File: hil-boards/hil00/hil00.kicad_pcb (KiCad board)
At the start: 2 copper layers, 80 x 25 mm, 35 parts, among them J1 USB_C_Receptacle_USB2.0, J2 Conn_01x05_Male, J3 Conn_01x05_Male, Q1 BC847, Q2 BC847, U1 ADUM4160, U2 AMS1117-3.3, U3 CH340G, Y1 Crystal

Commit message: all elements placed
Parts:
- added REF**: MountingHole_3.2mm_M3, MountingHole:MountingHole_3.2mm_M3, F.Cu at (177.0, 128.5)
- added REF**1: MountingHole_3.2mm_M3, MountingHole:MountingHole_3.2mm_M3, F.Cu at (166.8, 128.5)
- added REF**2: MountingHole_3.2mm_M3, MountingHole:MountingHole_3.2mm_M3, F.Cu at (156.7, 128.5)
- added REF**3: MountingHole_3.2mm_M3, MountingHole:MountingHole_3.2mm_M3, F.Cu at (146.5, 128.5)
- added REF**4: MountingHole_3.2mm_M3, MountingHole:MountingHole_3.2mm_M3, F.Cu at (136.4, 128.5)
- added REF**5: MountingHole_3.2mm_M3, MountingHole:MountingHole_3.2mm_M3, F.Cu at (126.2, 128.5)
- added REF**6: MountingHole_3.2mm_M3, MountingHole:MountingHole_3.2mm_M3, F.Cu at (116.0, 128.5)
- added REF**7: MountingHole_3.2mm_M3, MountingHole:MountingHole_3.2mm_M3, F.Cu at (105.9, 128.5)
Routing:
- removed copper zone on B.Cu, net GND1
- removed copper zone on F.Cu, net GND1
- removed copper zone on B.Cu, net GND2
- removed copper zone on F.Cu, net GND2
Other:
- board size 80 x 25 mm -> 82 x 30.5 mm

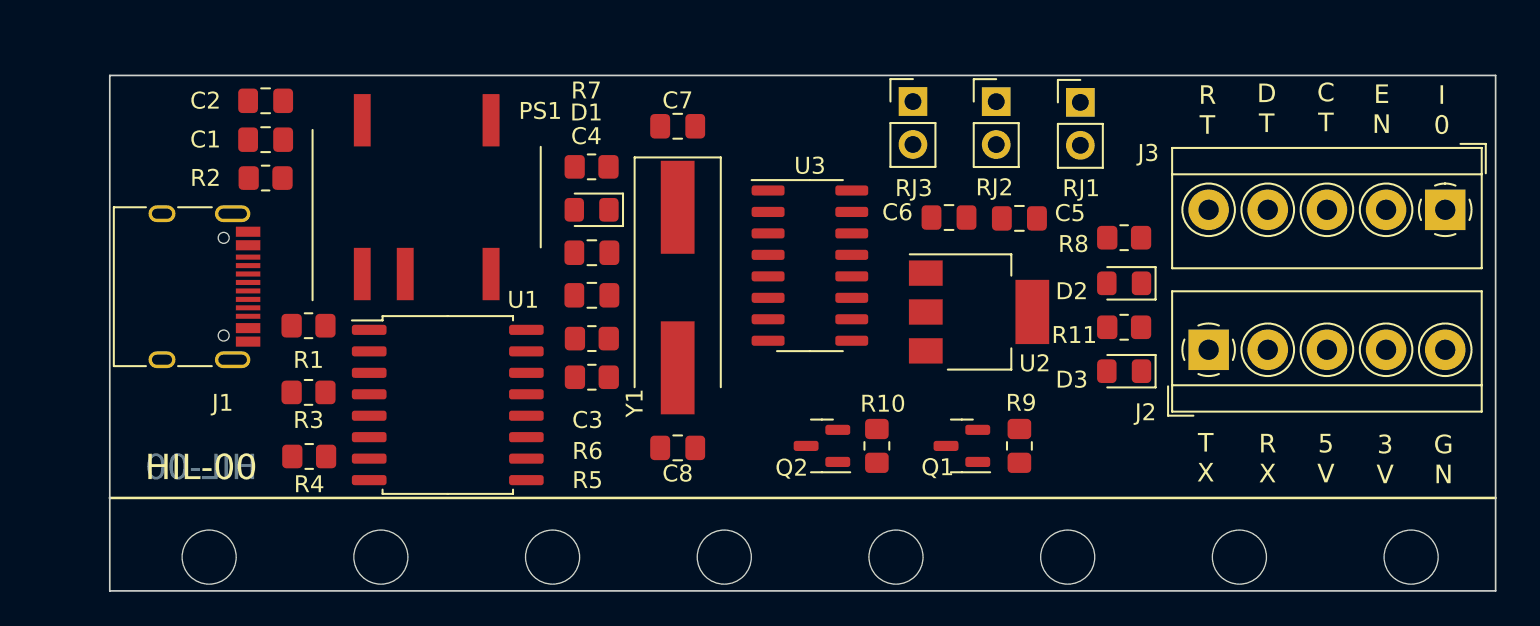
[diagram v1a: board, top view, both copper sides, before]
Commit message: all traces routed
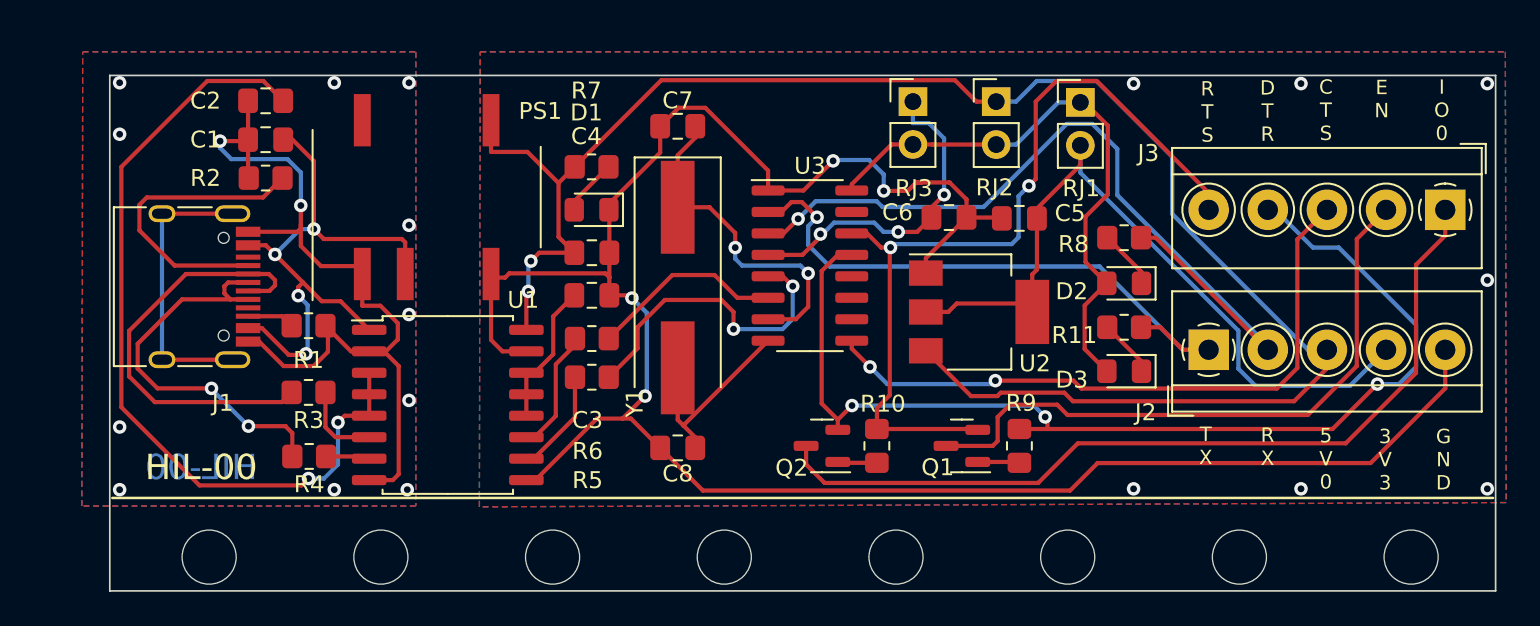
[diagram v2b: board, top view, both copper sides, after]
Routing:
- net GND2: track 0.00 -> 128.5 mm, vias 0 -> 11
- net +5V: track 0.00 -> 102.7 mm, vias 0 -> 2
- net /DTR: track 0.00 -> 64.7 mm, vias 0 -> 3
- net GND1: track 0.00 -> 52.1 mm, vias 0 -> 13
- net /IO0: track 0.00 -> 50.7 mm
- net /RTS: track 0.00 -> 50.5 mm, vias 0 -> 2
- net /RX: track 0.00 -> 50.1 mm, vias 0 -> 1
- net Net-(C2-Pad1): track 0.00 -> 48.7 mm, vias 0 -> 2
- net +3.3V: track 0.00 -> 44.7 mm
- net /CTS: track 0.00 -> 38.6 mm, vias 0 -> 2
- net /EN: track 0.00 -> 37.6 mm
- net /TX: track 0.00 -> 36.2 mm, vias 0 -> 1
- net Net-(C1-Pad1): track 0.00 -> 34.9 mm, vias 0 -> 4
- net VCC: track 0.00 -> 34.8 mm
- net Net-(J1-PadA7): track 0.00 -> 25.4 mm
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- added copper zone on B.Cu, net GND1
- added copper zone on F.Cu, net GND1
- added copper zone on B.Cu, net GND2
- added copper zone on F.Cu, net GND2
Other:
- board text added: "3 V 3"
- board text added: "5 V 0"
- board text added: "C T S"
- board text added: "D T R"
- board text added: "G N D"
- board text added: "I O 0"
- board text added: "R T S"
- board text removed: "3 V"
- board text removed: "5 V"
- board text removed: "C T"
- board text removed: "D T"
- board text removed: "G N"
- board text removed: "I 0"
- board text removed: "R T"

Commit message: improved vias on ground planes
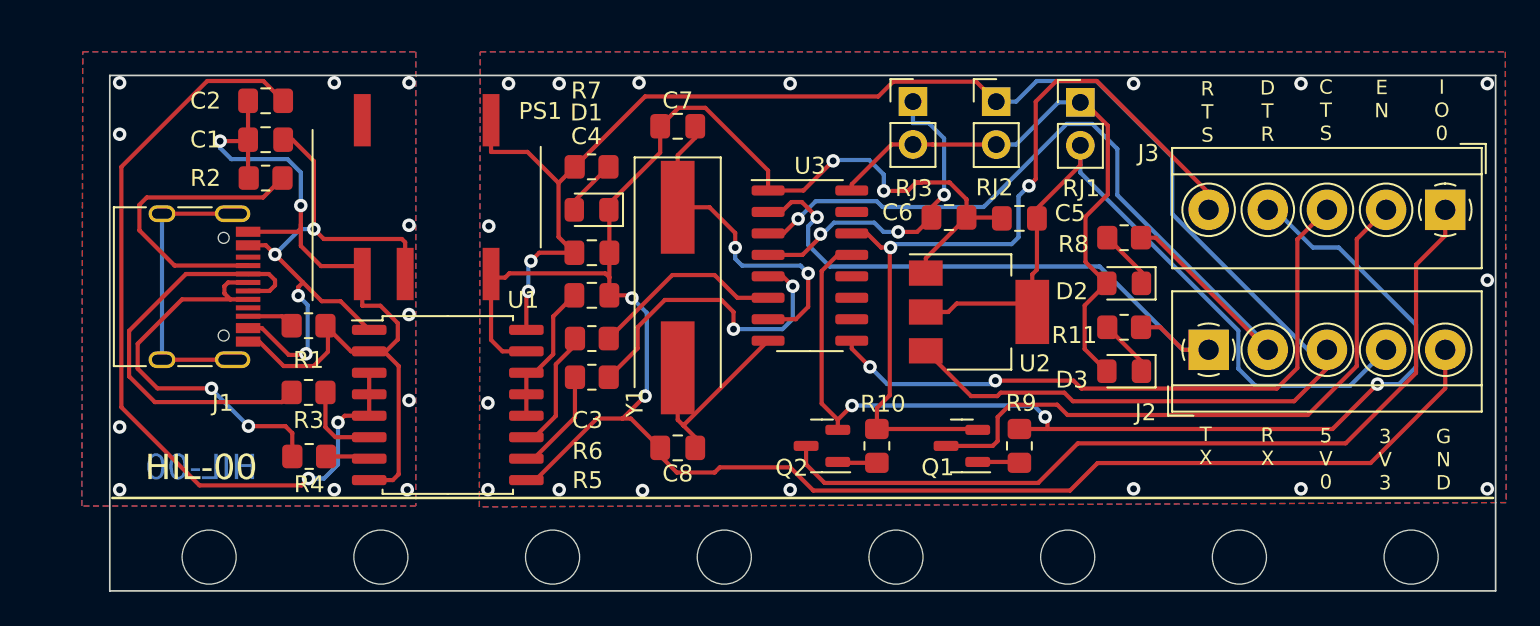
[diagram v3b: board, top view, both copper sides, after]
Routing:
- net GND2: track 128.5 -> 129.0 mm, vias 11 -> 21
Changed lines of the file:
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@@
   (segment (start 124.65 116.325) (end 123.2338 116.325) (width 0.25) (layer "F.Cu") (net 5))
   (segment (start 129.533 107.95) (end 129.533 107.5994) (width 0.25) (layer "F.Cu") (net 5))
-  (segment (start 156.8196 124.5616) (end 158.4452 122.936) (width 0.25) (layer "F.Cu") (net 5))
   (segment (start 123.64391 111.7092) (end 123.391555 111.961555) (width 0.25) (layer "F.Cu") (net 5))
   (segment (start 129.5615 107.9785) (end 129.5615 110.49) (width 0.25) (layer "F.Cu") (net 5))
@@
   (segment (start 123.2338 116.325) (end 122.56 115.6512) (width 0.25) (layer "F.Cu") (net 5))
   (segment (start 145.796 106.8324) (end 147.2184 106.8324) (width 0.25) (layer "F.Cu") (net 5))
+  (segment (start 132.5665 122.5081) (end 133.5532 123.4948) (width 0.25) (layer "F.Cu") (net 5))
+  (segment (start 135.7884 123.4948) (end 136.0932 123.19) (width 0.25) (layer "F.Cu") (net 5))
   (segment (start 130.8329 120.3034) (end 132.5665 122.037) (width 0.25) (layer "F.Cu") (net 5))
   (segment (start 147.7189 106.3319) (end 148.0237 106.3319) (width 0.25) (layer "F.Cu") (net 5))
   (segment (start 131.6736 118.9736) (end 130.3438 120.3034) (width 0.25) (layer "F.Cu") (net 5))
   (segment (start 125.1813 123.945) (end 128.8229 120.3034) (width 0.25) (layer "F.Cu") (net 5))
-  (segment (start 174.5996 122.936) (end 179.0192 118.5164) (width 0.25) (layer "F.Cu") (net 5))
-  (segment (start 179.0192 118.5164) (end 179.0192 116.232) (width 0.25) (layer "F.Cu") (net 5))
+  (segment (start 140.2588 123.19) (end 141.6304 124.5616) (width 0.25) (layer "F.Cu") (net 5))
+  (segment (start 132.5665 122.037) (end 132.5665 122.5081) (width 0.25) (layer "F.Cu") (net 5))
   (segment (start 122.771555 111.961555) (end 122.56 111.75) (width 0.25) (layer "F.Cu") (net 5))
   (segment (start 148.2848 111.6952) (end 148.2848 110.8167) (width 0.25) (layer "F.Cu") (net 5))
   (segment (start 142.7988 105.0544) (end 141.0462 106.807) (width 0.25) (layer "F.Cu") (net 5))
-  (segment (start 132.5665 122.037) (end 135.0911 124.5616) (width 0.25) (layer "F.Cu") (net 5))
   (segment (start 124.65 123.945) (end 125.1813 123.945) (width 0.25) (layer "F.Cu") (net 5))
   (segment (start 148.2848 110.8167) (end 150.6943 108.4072) (width 0.25) (layer "F.Cu") (net 5))
   (segment (start 132.5665 104.5659) (end 132.5665 103.007) (width 0.25) (layer "F.Cu") (net 5))
   (segment (start 129.5615 110.49) (end 129.5615 111.9509) (width 0.25) (layer "F.Cu") (net 5))
+  (segment (start 141.6304 124.5616) (end 156.8196 124.5616) (width 0.25) (layer "F.Cu") (net 5))
+  (segment (start 156.8196 124.5616) (end 158.4452 122.936) (width 0.25) (layer "F.Cu") (net 5))
   (segment (start 129.533 107.5994) (end 132.5665 104.5659) (width 0.25) (layer "F.Cu") (net 5))
   (segment (start 129.5615 111.9509) (end 129.3198 111.7092) (width 0.25) (layer "F.Cu") (net 5))
@@
   (segment (start 130.899301 113.170101) (end 130.7392 113.01) (width 0.25) (layer "F.Cu") (net 5))
   (segment (start 129.533 107.95) (end 129.5615 107.9785) (width 0.25) (layer "F.Cu") (net 5))
+  (segment (start 174.5996 122.936) (end 179.0192 118.5164) (width 0.25) (layer "F.Cu") (net 5))
   (segment (start 138.9522 105.6291) (end 135.2367 101.9136) (width 0.25) (layer "F.Cu") (net 5))
-  (segment (start 135.0911 124.5616) (end 156.8196 124.5616) (width 0.25) (layer "F.Cu") (net 5))
   (segment (start 147.2184 106.8324) (end 147.7189 106.3319) (width 0.25) (layer "F.Cu") (net 5))
   (segment (start 128.8229 120.3034) (end 130.3438 120.3034) (width 0.25) (layer "F.Cu") (net 5))
   (segment (start 141.0462 106.807) (end 138.9522 106.807) (width 0.25) (layer "F.Cu") (net 5))
+  (segment (start 179.0192 118.5164) (end 179.0192 116.232) (width 0.25) (layer "F.Cu") (net 5))
   (segment (start 129.3198 111.7092) (end 123.64391 111.7092) (width 0.25) (layer "F.Cu") (net 5))
   (segment (start 152.7341 108.4072) (end 152.7849 108.458) (width 0.25) (layer "F.Cu") (net 5))
-  (segment (start 158.4452 122.936) (end 174.5996 122.936) (width 0.25) (layer "F.Cu") (net 5))
+  (segment (start 136.0932 123.19) (end 140.2588 123.19) (width 0.25) (layer "F.Cu") (net 5))
+  (segment (start 133.5532 123.4948) (end 135.7884 123.4948) (width 0.25) (layer "F.Cu") (net 5))
   (segment (start 138.9522 106.807) (end 138.9522 105.6291) (width 0.25) (layer "F.Cu") (net 5))
   (segment (start 150.6943 107.334) (end 149.6922 106.3319) (width 0.25) (layer "F.Cu") (net 5))
+  (segment (start 158.4452 122.936) (end 174.5996 122.936) (width 0.25) (layer "F.Cu") (net 5))
   (segment (start 123.391555 111.961555) (end 122.771555 111.961555) (width 0.25) (layer "F.Cu") (net 5))
   (segment (start 130.7392 113.01) (end 129.5615 113.01) (width 0.25) (layer "F.Cu") (net 5))
@@
   (via (at 131.6736 118.9736) (size 0.8) (drill 0.4) (layers "F.Cu" "B.Cu") (net 5))
   (via (at 160.5788 124.46) (size 0.8) (drill 0.4) (layers "F.Cu" "B.Cu") (free) (net 5))
+  (via (at 122.428 108.9152) (size 0.8) (drill 0.4) (layers "F.Cu" "B.Cu") (free) (net 5))
+  (via (at 140.2588 100.4824) (size 0.8) (drill 0.4) (layers "F.Cu" "B.Cu") (free) (net 5))
   (via (at 145.796 106.8324) (size 0.8) (drill 0.4) (layers "F.Cu" "B.Cu") (net 5))
+  (via (at 131.5212 124.5616) (size 0.8) (drill 0.4) (layers "F.Cu" "B.Cu") (free) (net 5))
   (via (at 170.4848 124.46) (size 0.8) (drill 0.4) (layers "F.Cu" "B.Cu") (free) (net 5))
+  (via (at 126.5936 124.5108) (size 0.8) (drill 0.4) (layers "F.Cu" "B.Cu") (free) (net 5))
+  (via (at 131.318 100.4316) (size 0.8) (drill 0.4) (layers "F.Cu" "B.Cu") (free) (net 5))
+  (via (at 123.5964 100.4824) (size 0.8) (drill 0.4) (layers "F.Cu" "B.Cu") (free) (net 5))
+  (via (at 122.3772 124.5108) (size 0.8) (drill 0.4) (layers "F.Cu" "B.Cu") (free) (net 5))
   (via (at 160.5788 100.4824) (size 0.8) (drill 0.4) (layers "F.Cu" "B.Cu") (free) (net 5))
   (via (at 181.5084 100.4824) (size 0.8) (drill 0.4) (layers "F.Cu" "B.Cu") (free) (net 5))
   (via (at 130.899301 113.170101) (size 0.8) (drill 0.4) (layers "F.Cu" "B.Cu") (net 5))
   (via (at 170.4848 100.4824) (size 0.8) (drill 0.4) (layers "F.Cu" "B.Cu") (free) (net 5))
+  (via (at 140.2588 124.5108) (size 0.8) (drill 0.4) (layers "F.Cu" "B.Cu") (free) (net 5))
   (via (at 142.7988 105.0544) (size 0.8) (drill 0.4) (layers "F.Cu" "B.Cu") (net 5))
+  (via (at 122.3772 119.38) (size 0.8) (drill 0.4) (layers "F.Cu" "B.Cu") (free) (net 5))
   (via (at 181.5084 124.46) (size 0.8) (drill 0.4) (layers "F.Cu" "B.Cu") (free) (net 5))
   (via (at 181.5084 112.1156) (size 0.8) (drill 0.4) (layers "F.Cu" "B.Cu") (free) (net 5))
+  (via (at 126.5936 100.4824) (size 0.8) (drill 0.4) (layers "F.Cu" "B.Cu") (free) (net 5))
   (segment (start 142.8496 105.0036) (end 142.7988 105.0544) (width 0.25) (layer "B.Cu") (net 5))
   (segment (start 131.6736 118.9736) (end 131.7752 118.872) (width 0.25) (layer "B.Cu") (net 5))
@@
   (segment (start 124.65 121.405) (end 125.1361 121.405) (width 0.25) (layer "F.Cu") (net 32))
   (segment (start 127.524 115.9604) (end 127.524 115.57) (width 0.25) (layer "F.Cu") (net 32))
+  (segment (start 127.508 105.41) (end 131.6736 101.2444) (width 0.25) (layer "F.Cu") (net 33))
   (segment (start 152.510905 118.9736) (end 150.9632 118.9736) (width 0.25) (layer "F.Cu") (net 33))
   (segment (start 172.0192 116.232) (end 172.0192 117.3376) (width 0.25) (layer "F.Cu") (net 33))
+  (segment (start 151.2708 100.3692) (end 152.4508 101.5492) (width 0.25) (layer "F.Cu") (net 33))
+  (segment (start 131.6736 101.2444) (end 145.473 101.2444) (width 0.25) (layer "F.Cu") (net 33))
   (segment (start 126.5539 106.3641) (end 127.508 105.41) (width 0.25) (layer "F.Cu") (net 33))
   (segment (start 124.65 112.8908) (end 124.7648 112.776) (width 0.25) (layer "F.Cu") (net 33))
-  (segment (start 132.6388 100.2792) (end 150.0055 100.2792) (width 0.25) (layer "F.Cu") (net 33))
-  (segment (start 150.0055 100.2792) (end 151.2755 101.5492) (width 0.25) (layer "F.Cu") (net 33))
   (segment (start 172.0192 117.3376) (end 170.0784 119.2784) (width 0.25) (layer "F.Cu") (net 33))
   (segment (start 122.56 104.5253) (end 124.7151 104.5253) (width 0.25) (layer "F.Cu") (net 33))
   (segment (start 126.5539 109.5574) (end 126.5539 106.3641) (width 0.25) (layer "F.Cu") (net 33))
   (segment (start 150.9632 118.9736) (end 148.2848 116.2952) (width 0.25) (layer "F.Cu") (net 33))
-  (segment (start 151.2755 101.5492) (end 152.4508 101.5492) (width 0.25) (layer "F.Cu") (net 33))
+  (segment (start 146.3482 100.3692) (end 151.2708 100.3692) (width 0.25) (layer "F.Cu") (net 33))
   (segment (start 156.4824 118.7704) (end 152.714105 118.7704) (width 0.25) (layer "F.Cu") (net 33))
+  (segment (start 145.473 101.2444) (end 146.3482 100.3692) (width 0.25) (layer "F.Cu") (net 33))
   (segment (start 124.9172 110.9847) (end 125.4119 110.49) (width 0.25) (layer "F.Cu") (net 33))
   (segment (start 124.7151 104.5253) (end 126.5539 106.3641) (width 0.25) (layer "F.Cu") (net 33))
   (segment (start 170.0784 119.2784) (end 156.9904 119.2784) (width 0.25) (layer "F.Cu") (net 33))
-  (segment (start 127.508 105.41) (end 132.6388 100.2792) (width 0.25) (layer "F.Cu") (net 33))
   (segment (start 122.56 102.65) (end 122.56 104.5253) (width 0.25) (layer "F.Cu") (net 33))
   (segment (start 125.4119 110.49) (end 127.4865 110.49) (width 0.25) (layer "F.Cu") (net 33))

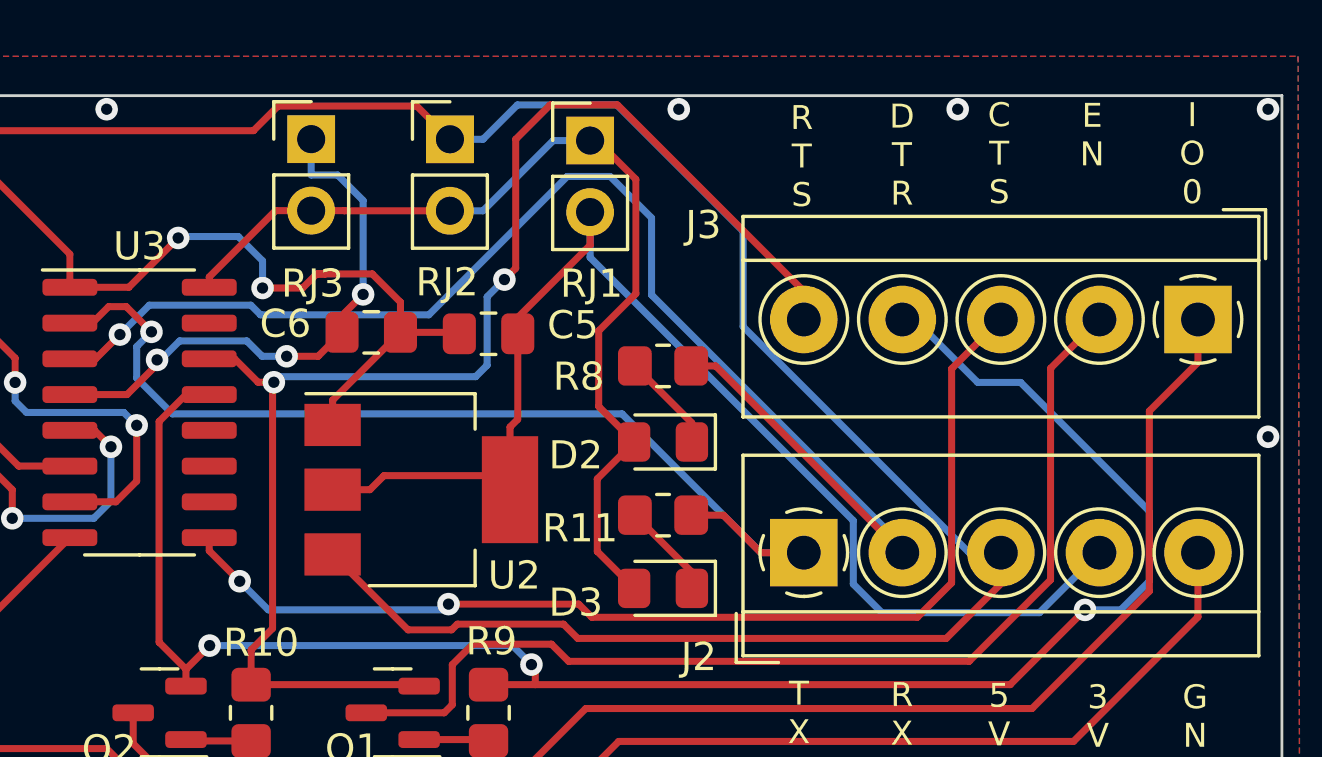
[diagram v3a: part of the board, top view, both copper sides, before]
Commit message: improved vias on ground planes++
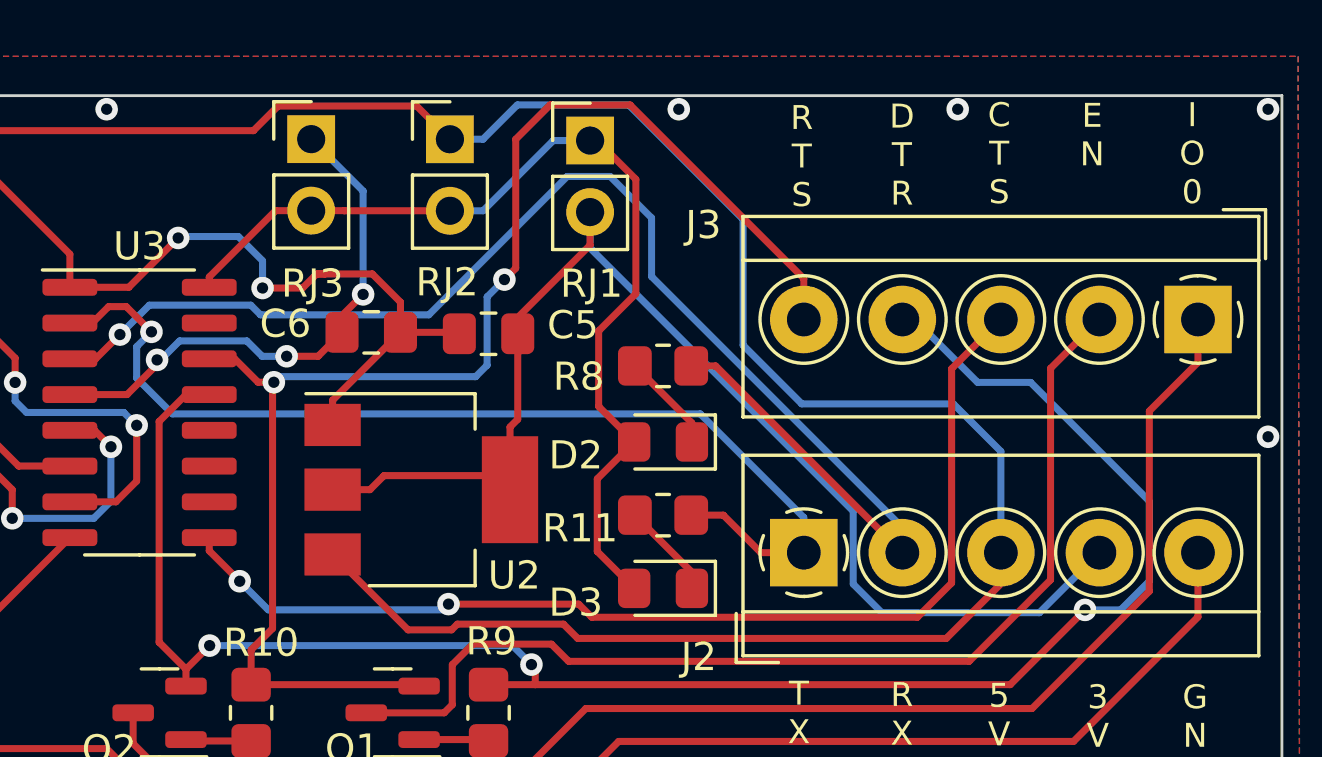
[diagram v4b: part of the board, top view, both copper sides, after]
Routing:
- net +5V: track 102.7 -> 105.4 mm
- net /TX: track 36.2 -> 36.9 mm
- net Net-(C6-Pad1): track 19.6 -> 19.1 mm
